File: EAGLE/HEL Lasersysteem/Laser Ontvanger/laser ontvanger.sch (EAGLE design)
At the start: 13 parts, among them IC1 HS0038A2, IC2 74LVC1G14DBV, IC3 74LVC1G14DBV

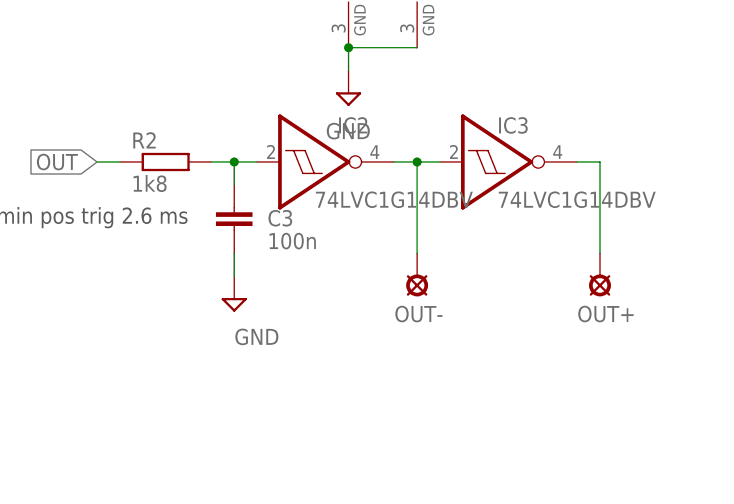
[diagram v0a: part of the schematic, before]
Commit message: Laser PCB's aangepast
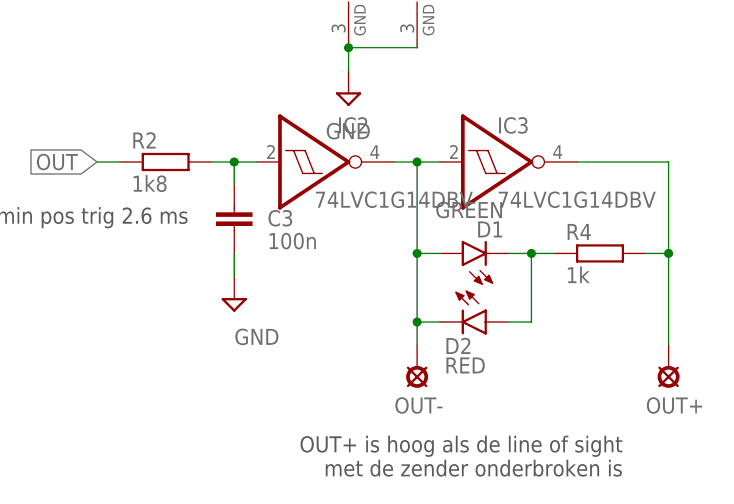
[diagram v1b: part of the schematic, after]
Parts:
- added D1: GREEN, led:LEDCHIP-LED0805
- added D2: RED, led:LEDCHIP-LED0805
- added R4: 1k, rcl:R-EU_R0805
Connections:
- new net N$2: D1.C, D2.A, R4.1
- net N$3: now also D1.A, D2.C
- net N$4: now also R4.2
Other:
- note added: "OUT+ is hoog als de line of sight met de zender onderbroken is"
- moved on the sheet: OUT+, OUT-
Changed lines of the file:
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@@
 <part name="SUPPLY3" library="supply2" library_urn="urn:adsk.eagle:library:372" deviceset="GND" device=""/>
 <part name="R3" library="rcl" library_urn="urn:adsk.eagle:library:334" deviceset="R-EU_" device="R0805" package3d_urn="urn:adsk.eagle:package:23553/2" value="optional"/>
+<part name="D1" library="led" library_urn="urn:adsk.eagle:library:259" deviceset="LED" device="CHIP-LED0805" package3d_urn="urn:adsk.eagle:package:15818/2" value="GREEN"/>
+<part name="D2" library="led" library_urn="urn:adsk.eagle:library:259" deviceset="LED" device="CHIP-LED0805" package3d_urn="urn:adsk.eagle:package:15818/2" value="RED"/>
+<part name="R4" library="rcl" library_urn="urn:adsk.eagle:library:334" deviceset="R-EU_" device="R0805" package3d_urn="urn:adsk.eagle:package:23553/2" value="1k"/>
 </parts>
 <sheets>
@@
 <text x="-2.54" y="40.64" size="1.778" layer="97">Als de TSOP module ontvangt gaat de output omlaag</text>
 <text x="83.82" y="58.42" size="1.778" layer="97" rot="R180">min pos trig 2.6 ms</text>
+<text x="132.08" y="33.02" size="1.778" layer="97" rot="R180">OUT+ is hoog als de line of sight
+met de zender onderbroken is</text>
 </plain>
 <instances>
@@
 <attribute name="VALUE" x="-1.27" y="54.61" size="1.778" layer="96"/>
 </instance>
-<instance part="OUT+" gate="1" x="129.54" y="50.8" smashed="yes" rot="R180">
-<attribute name="NAME" x="127" y="45.72" size="1.778" layer="95"/>
+<instance part="OUT+" gate="1" x="137.16" y="40.64" smashed="yes" rot="R180">
+<attribute name="NAME" x="134.62" y="35.56" size="1.778" layer="95"/>
 </instance>
 <instance part="P+2" gate="VCC" x="101.6" y="96.52" smashed="yes">
@@
 <attribute name="VALUE" x="99.06" y="66.04" size="1.778" layer="96"/>
 </instance>
-<instance part="OUT-" gate="1" x="109.22" y="50.8" smashed="yes" rot="R180">
-<attribute name="NAME" x="106.68" y="45.72" size="1.778" layer="95"/>
+<instance part="OUT-" gate="1" x="109.22" y="40.64" smashed="yes" rot="R180">
+<attribute name="NAME" x="106.68" y="35.56" size="1.778" layer="95"/>
 </instance>
 <instance part="IC2" gate="A" x="96.52" y="63.5" smashed="yes">
@@
 <attribute name="NAME" x="18.8214" y="67.31" size="1.778" layer="95" rot="R90"/>
 <attribute name="VALUE" x="23.622" y="67.31" size="1.778" layer="96" rot="R90"/>
+</instance>
+<instance part="D1" gate="G$1" x="114.3" y="53.34" smashed="yes" rot="R90">
+<attribute name="NAME" x="118.872" y="56.896" size="1.778" layer="95" rot="R180"/>
+<attribute name="VALUE" x="118.872" y="59.055" size="1.778" layer="96" rot="R180"/>
+</instance>
+<instance part="D2" gate="G$1" x="116.84" y="45.72" smashed="yes" rot="R270">
+<attribute name="NAME" x="112.268" y="42.164" size="1.778" layer="95"/>
+<attribute name="VALUE" x="112.268" y="40.005" size="1.778" layer="96"/>
+</instance>
+<instance part="R4" gate="G$1" x="129.54" y="53.34" smashed="yes">
+<attribute name="NAME" x="125.73" y="54.8386" size="1.778" layer="95"/>
+<attribute name="VALUE" x="125.73" y="50.038" size="1.778" layer="96"/>
 </instance>
 </instances>
@@
 <wire x1="109.22" y1="63.5" x2="111.76" y2="63.5" width="0.1524" layer="91"/>
 <pinref part="OUT-" gate="1" pin="MP"/>
+<wire x1="109.22" y1="43.18" x2="109.22" y2="45.72" width="0.1524" layer="91"/>
+<pinref part="IC2" gate="A" pin="O"/>
+<wire x1="109.22" y1="45.72" x2="109.22" y2="53.34" width="0.1524" layer="91"/>
 <wire x1="109.22" y1="53.34" x2="109.22" y2="63.5" width="0.1524" layer="91"/>
-<pinref part="IC2" gate="A" pin="O"/>
 <wire x1="109.22" y1="63.5" x2="106.68" y2="63.5" width="0.1524" layer="91"/>
 <junction x="109.22" y="63.5"/>
+<pinref part="D2" gate="G$1" pin="C"/>
+<wire x1="111.76" y1="45.72" x2="109.22" y2="45.72" width="0.1524" layer="91"/>
+<junction x="109.22" y="45.72"/>
+<pinref part="D1" gate="G$1" pin="A"/>
+<wire x1="111.76" y1="53.34" x2="109.22" y2="53.34" width="0.1524" layer="91"/>
+<junction x="109.22" y="53.34"/>
 </segment>
 </net>
@@
 <segment>
 <pinref part="OUT+" gate="1" pin="MP"/>
-<wire x1="129.54" y1="53.34" x2="129.54" y2="63.5" width="0.1524" layer="91"/>
+<wire x1="137.16" y1="43.18" x2="137.16" y2="53.34" width="0.1524" layer="91"/>
 <pinref part="IC3" gate="A" pin="O"/>
-<wire x1="129.54" y1="63.5" x2="127" y2="63.5" width="0.1524" layer="91"/>
+<wire x1="137.16" y1="53.34" x2="137.16" y2="63.5" width="0.1524" layer="91"/>
+<wire x1="137.16" y1="63.5" x2="127" y2="63.5" width="0.1524" layer="91"/>
+<pinref part="R4" gate="G$1" pin="2"/>
+<wire x1="134.62" y1="53.34" x2="137.16" y2="53.34" width="0.1524" layer="91"/>
+<junction x="137.16" y="53.34"/>
 </segment>
 </net>
@@
 </segment>
 </net>
+<net name="N$2" class="0">
+<segment>
+<pinref part="D1" gate="G$1" pin="C"/>
+<pinref part="R4" gate="G$1" pin="1"/>
+<wire x1="119.38" y1="53.34" x2="121.92" y2="53.34" width="0.1524" layer="91"/>
+<wire x1="121.92" y1="53.34" x2="124.46" y2="53.34" width="0.1524" layer="91"/>
+<wire x1="121.92" y1="53.34" x2="121.92" y2="45.72" width="0.1524" layer="91"/>
+<junction x="121.92" y="53.34"/>
+<pinref part="D2" gate="G$1" pin="A"/>
+<wire x1="121.92" y1="45.72" x2="119.38" y2="45.72" width="0.1524" layer="91"/>
+</segment>
+</net>
 </nets>
 </sheet>
@@
 </drawing>
 <compatibility>
+<note version="6.3" minversion="6.2.2" severity="warning">
+Since Version 6.2.2 text objects can contain more than one line,
+which will not be processed correctly with this version.
+</note>
 <note version="8.2" severity="warning">
 Since Version 8.2, EAGLE supports online libraries. The ids
